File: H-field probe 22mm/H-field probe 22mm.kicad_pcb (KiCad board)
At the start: 4 copper layers, 98.8 x 48 mm, 1 part, among them J1 Conn_Coaxial

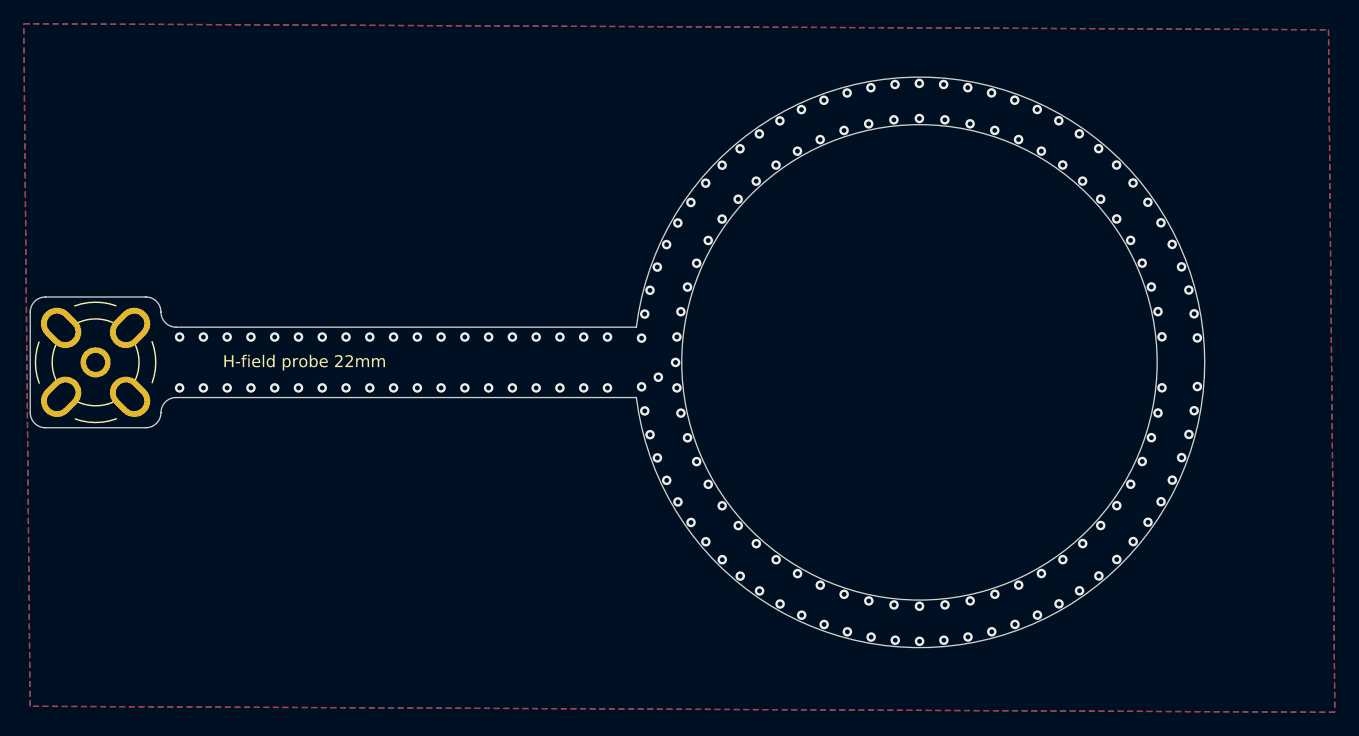
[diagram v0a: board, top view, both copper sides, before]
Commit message: Fixed wrong diamter. Changed via size. Added text and logo
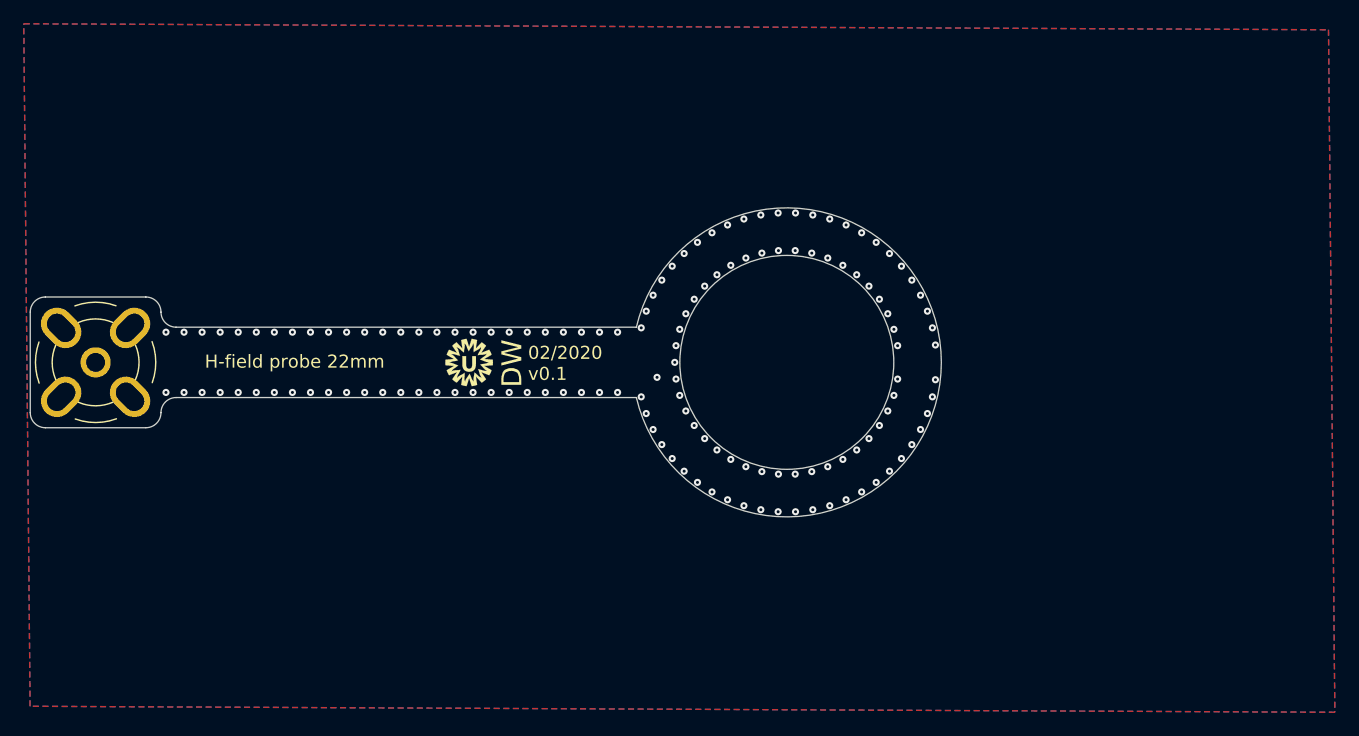
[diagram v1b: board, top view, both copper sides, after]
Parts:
- added G***: LOGO, _Custom:UMC_logo_4mm, F.Cu at (142.3, 96.3)
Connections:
- J1 pad 1: Net-(J1-Pad1) -> GND
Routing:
- net Net-(J1-Pad1): track 47.3 -> 0.00 mm
- net GND: track 0.00 -> 47.2 mm, vias 168 -> 144
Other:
- board size 98.8 x 48 mm -> 76.7 x 26 mm
- rule via_min_drill: 0.3 -> 0.25
- board text added: "02/2020 v0.1"
- board text added: "DW"

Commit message: Updated connector
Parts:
- turned J1 to 270 degrees
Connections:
- J1 pad 1: GND -> Net-(J1-Pad1)
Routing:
- net Net-(J1-Pad1): track 0.00 -> 47.2 mm
- net GND: track 47.2 -> 0.00 mm
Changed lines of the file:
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@@
     (zones 0)
     (modules 2)
-    (nets 2)
+    (nets 3)
   )
   (page A4)
@@
   (net 0 "")
   (net 1 GND)
+  (net 2 "Net-(J1-Pad1)")
   (net_class Default "This is the default net class."
     (clearance 0.1)
@@
     (uvia_drill 0.1)
     (add_net GND)
+    (add_net "Net-(J1-Pad1)")
+  )
+  (module _Custom:BNC_SMA_Vertical (layer F.Cu)
+    (at 110.88 96.27 270)
+    (descr "BNC female PCB mount 4 pin straight chassis connector http://www.te.com/usa-en/product-1-1478204-0.html")
+    (tags "BNC female PCB mount 4 pin straight chassis connector ")
+    (fp_text reference J1 (at -4.32 0) (layer F.SilkS) hide
+      (effects (font (size 1 1) (thickness 0.15)))
+    )
+    (fp_text value Conn_Coaxial (at 0 6.5 90) (layer F.Fab)
+      (effects (font (size 1 1) (thickness 0.15)))
+    )
+    (fp_line (start -2.54 5.08) (end 2.54 5.08) (layer F.SilkS) (width 0.12))
+    (fp_text user %R (at 0 0 90) (layer F.Fab)
+      (effects (font (size 1 1) (thickness 0.15)))
+    )
+    (fp_line (start 5.5 -5.5) (end 5.5 5.5) (layer F.CrtYd) (width 0.05))
+    (fp_line (start 5.5 5.5) (end -5.5 5.5) (layer F.CrtYd) (width 0.05))
+    (fp_line (start -5.5 5.5) (end -5.5 -5.5) (layer F.CrtYd) (width 0.05))
+    (fp_line (start -5.5 -5.5) (end 5.5 -5.5) (layer F.CrtYd) (width 0.05))
+    (fp_circle (center 0 0) (end 4.8 0) (layer F.Fab) (width 0.1))
+    (fp_arc (start 0 0) (end -4.75 1.75) (angle 40) (layer F.SilkS) (width 0.12))
+    (fp_arc (start 0 0) (end 4.75 -1.75) (angle 40) (layer F.SilkS) (width 0.12))
+    (fp_arc (start 0 0) (end -1.75 -4.75) (angle 40) (layer F.SilkS) (width 0.12))
+    (fp_circle (center 0 0) (end 3.175 0) (layer F.Fab) (width 0.1))
+    (fp_arc (start 0 0) (end 3.355 -1.45) (angle 46.74710926) (layer F.SilkS) (width 0.12))
+    (fp_arc (start 0 0) (end -3.355 1.45) (angle 46.74710926) (layer F.SilkS) (width 0.12))
+    (fp_arc (start 0 0) (end -1.45 -3.355) (angle 46.74710926) (layer F.SilkS) (width 0.12))
+    (fp_arc (start 0 0) (end 1.45 3.355) (angle 46.74710926) (layer F.SilkS) (width 0.12))
+    (pad 2 thru_hole oval (at -2.9 -2.9 315) (size 2.7 3.7) (drill oval 1.7 2.7) (layers *.Cu *.Mask)
+      (net 1 GND))
+    (pad 1 thru_hole circle (at 0 0 270) (size 2.54 2.54) (drill 1.6) (layers *.Cu *.Mask)
+      (net 2 "Net-(J1-Pad1)"))
+    (pad 2 thru_hole oval (at 2.9 -2.9 225) (size 2.7 3.7) (drill oval 1.7 2.7) (layers *.Cu *.Mask)
+      (net 1 GND))
+    (pad 2 thru_hole oval (at -2.9 2.9 225) (size 2.7 3.7) (drill oval 1.7 2.7) (layers *.Cu *.Mask)
+      (net 1 GND))
+    (pad 2 thru_hole oval (at 2.9 2.9 315) (size 2.7 3.7) (drill oval 1.7 2.7) (layers *.Cu *.Mask)
+      (net 1 GND))
+    (model :_Custom_3D:BNC_73171-3356.stp
+      (offset (xyz 0 -22.7 6.1))
+      (scale (xyz 1 1 1))
+      (rotate (xyz -90 0 0))
+    )
   )
   (module _Custom:UMC_logo_4mm (layer F.Cu)
@@
       (xy 0.212034 -1.990841)) (layer F.SilkS) (width 0.01))
   )
-  (module _Custom:BNC_SMA_Vertical (layer F.Cu)
-    (at 110.88 96.27)
-    (descr "BNC female PCB mount 4 pin straight chassis connector http://www.te.com/usa-en/product-1-1478204-0.html")
-    (tags "BNC female PCB mount 4 pin straight chassis connector ")
-    (fp_text reference J1 (at -4.32 0 90) (layer F.SilkS) hide
-      (effects (font (size 1 1) (thickness 0.15)))
-    )
-    (fp_text value Conn_Coaxial (at 0 6.5) (layer F.Fab)
-      (effects (font (size 1 1) (thickness 0.15)))
-    )
-    (fp_arc (start 0 0) (end 1.45 3.355) (angle 46.74710926) (layer F.SilkS) (width 0.12))
-    (fp_arc (start 0 0) (end -1.45 -3.355) (angle 46.74710926) (layer F.SilkS) (width 0.12))
-    (fp_arc (start 0 0) (end -3.355 1.45) (angle 46.74710926) (layer F.SilkS) (width 0.12))
-    (fp_arc (start 0 0) (end 3.355 -1.45) (angle 46.74710926) (layer F.SilkS) (width 0.12))
-    (fp_circle (center 0 0) (end 3.175 0) (layer F.Fab) (width 0.1))
-    (fp_arc (start 0 0) (end -1.75 -4.75) (angle 40) (layer F.SilkS) (width 0.12))
-    (fp_arc (start 0 0) (end 4.75 -1.75) (angle 40) (layer F.SilkS) (width 0.12))
-    (fp_arc (start 0 0) (end 1.75 4.75) (angle 40) (layer F.SilkS) (width 0.12))
-    (fp_arc (start 0 0) (end -4.75 1.75) (angle 40) (layer F.SilkS) (width 0.12))
-    (fp_circle (center 0 0) (end 4.8 0) (layer F.Fab) (width 0.1))
-    (fp_line (start -5.5 -5.5) (end 5.5 -5.5) (layer F.CrtYd) (width 0.05))
-    (fp_line (start -5.5 5.5) (end -5.5 -5.5) (layer F.CrtYd) (width 0.05))
-    (fp_line (start 5.5 5.5) (end -5.5 5.5) (layer F.CrtYd) (width 0.05))
-    (fp_line (start 5.5 -5.5) (end 5.5 5.5) (layer F.CrtYd) (width 0.05))
-    (fp_text user %R (at 0 0) (layer F.Fab)
-      (effects (font (size 1 1) (thickness 0.15)))
-    )
-    (pad 2 thru_hole oval (at 2.9 2.9 45) (size 2.7 3.7) (drill oval 1.7 2.7) (layers *.Cu *.Mask)
-      (net 1 GND))
-    (pad 2 thru_hole oval (at -2.9 2.9 315) (size 2.7 3.7) (drill oval 1.7 2.7) (layers *.Cu *.Mask)
-      (net 1 GND))
-    (pad 2 thru_hole oval (at 2.9 -2.9 315) (size 2.7 3.7) (drill oval 1.7 2.7) (layers *.Cu *.Mask)
-      (net 1 GND))
-    (pad 1 thru_hole circle (at 0 0) (size 2.54 2.54) (drill 1.6) (layers *.Cu *.Mask)
-      (net 1 GND) (clearance 0.2))
-    (pad 2 thru_hole oval (at -2.9 -2.9 45) (size 2.7 3.7) (drill oval 1.7 2.7) (layers *.Cu *.Mask)
-      (net 1 GND))
-    (model ${KISYS3DMOD}/Connector_Coaxial.3dshapes/BNC_TEConnectivity_1478204_Vertical.wrl
-      (at (xyz 0 0 0))
-      (scale (xyz 1 1 1))
-      (rotate (xyz 0 0 0))
-    )
-  )
   (dimension 2.96 (width 0.15) (layer Cmts.User)
     (gr_text "2.960 mm" (at 117.925 94.79 90) (layer Cmts.User)
@@
   (via (at 118.32 93.73) (size 0.6) (drill 0.25) (layers F.Cu B.Cu) (net 1))
   (via (at 154.8 98.8) (size 0.6) (drill 0.25) (layers F.Cu B.Cu) (net 1))
-  (segment (start 110.88 96.27) (end 158.04 96.27) (width 0.23495) (layer In1.Cu) (net 1))
   (via (at 158.12 97.53) (size 0.6) (drill 0.25) (layers F.Cu B.Cu) (net 1))
   (via (at 159.61 96.27) (size 0.6) (drill 0.25) (layers F.Cu B.Cu) (net 1))
@@
   (via (at 160.028948 93.490459) (size 0.6) (drill 0.25) (layers F.Cu B.Cu) (net 1))
   (via (at 159.715325 94.864531) (size 0.6) (drill 0.25) (layers F.Cu B.Cu) (net 1))
+  (segment (start 110.88 96.27) (end 158.04 96.27) (width 0.23495) (layer In1.Cu) (net 2))
   (zone (net 1) (net_name GND) (layer F.Cu) (hatch edge 0.508)
     (connect_pads (clearance 0))
